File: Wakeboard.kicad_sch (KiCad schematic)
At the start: 30 parts, among them CN1 JST S2B-PH-SM4-TB(LF)(SN), J2 HCTL HC-TYPE-C-16P-01A, Q1 DMP2045UQ-7, SW1 TS-1088-AR02016, SW2 TS-1088-AR02016, U1 RT9080-33GJ5, U2 ESP32-S3-MINI-1, U3 LIS3DHTR_C15134, U4 MCP73831T-2ACI/OT

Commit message: PCB and Schematic v1.0
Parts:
- added C7: 10uF, Capacitor_SMD:C_0805_2012Metric, symbol Device:C
- added C8: 0.1uF, Capacitor_SMD:C_0805_2012Metric, symbol Device:C
- added TP1, TP2: TestPoint, TestPoint:TestPoint_Pad_D1.5mm, symbol Connector:TestPoint
- renumbered SW2 to SW1, SW1 to SW2
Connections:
- net 3.3V: now also C7.1, C8.1, TP2.1
- net GND: now also C7.2, C8.2
- net GPIO1: now also U2.5 (IO1); no longer U2.15 (IO11)
- net at C1.1, D1.1 (K), Q1.2 (S)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: now also TP1.1

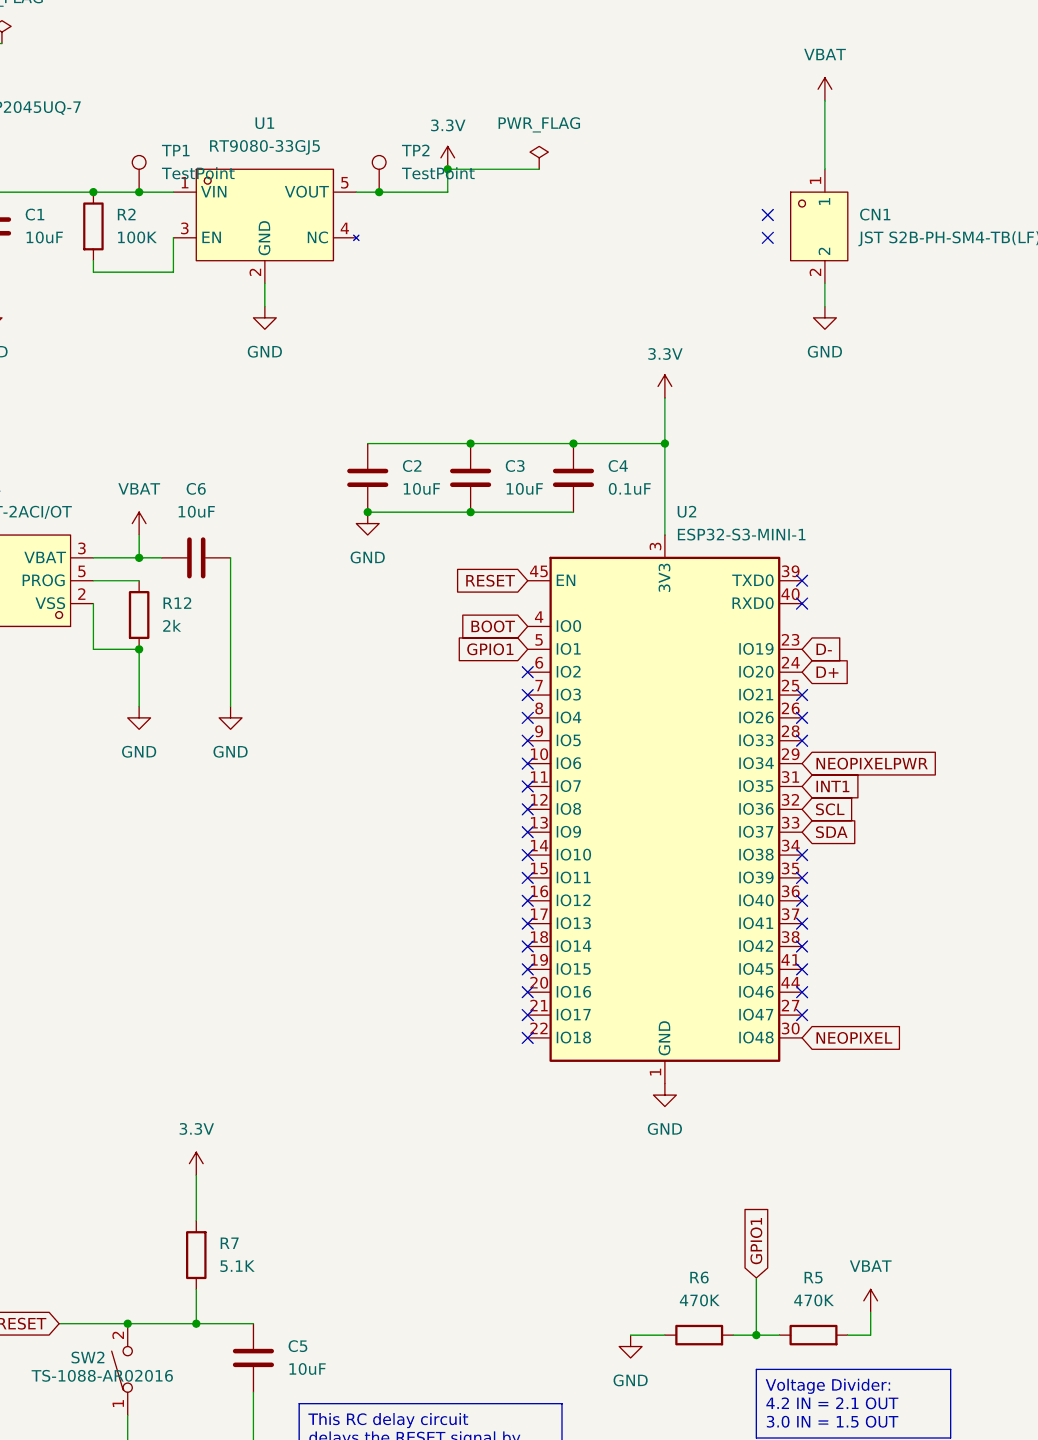
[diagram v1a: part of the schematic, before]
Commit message: Remove PCB below antenna. Swap SDA and SCL GPIO. Update interrupt to GPIO 21, battery level to GPIO 10.
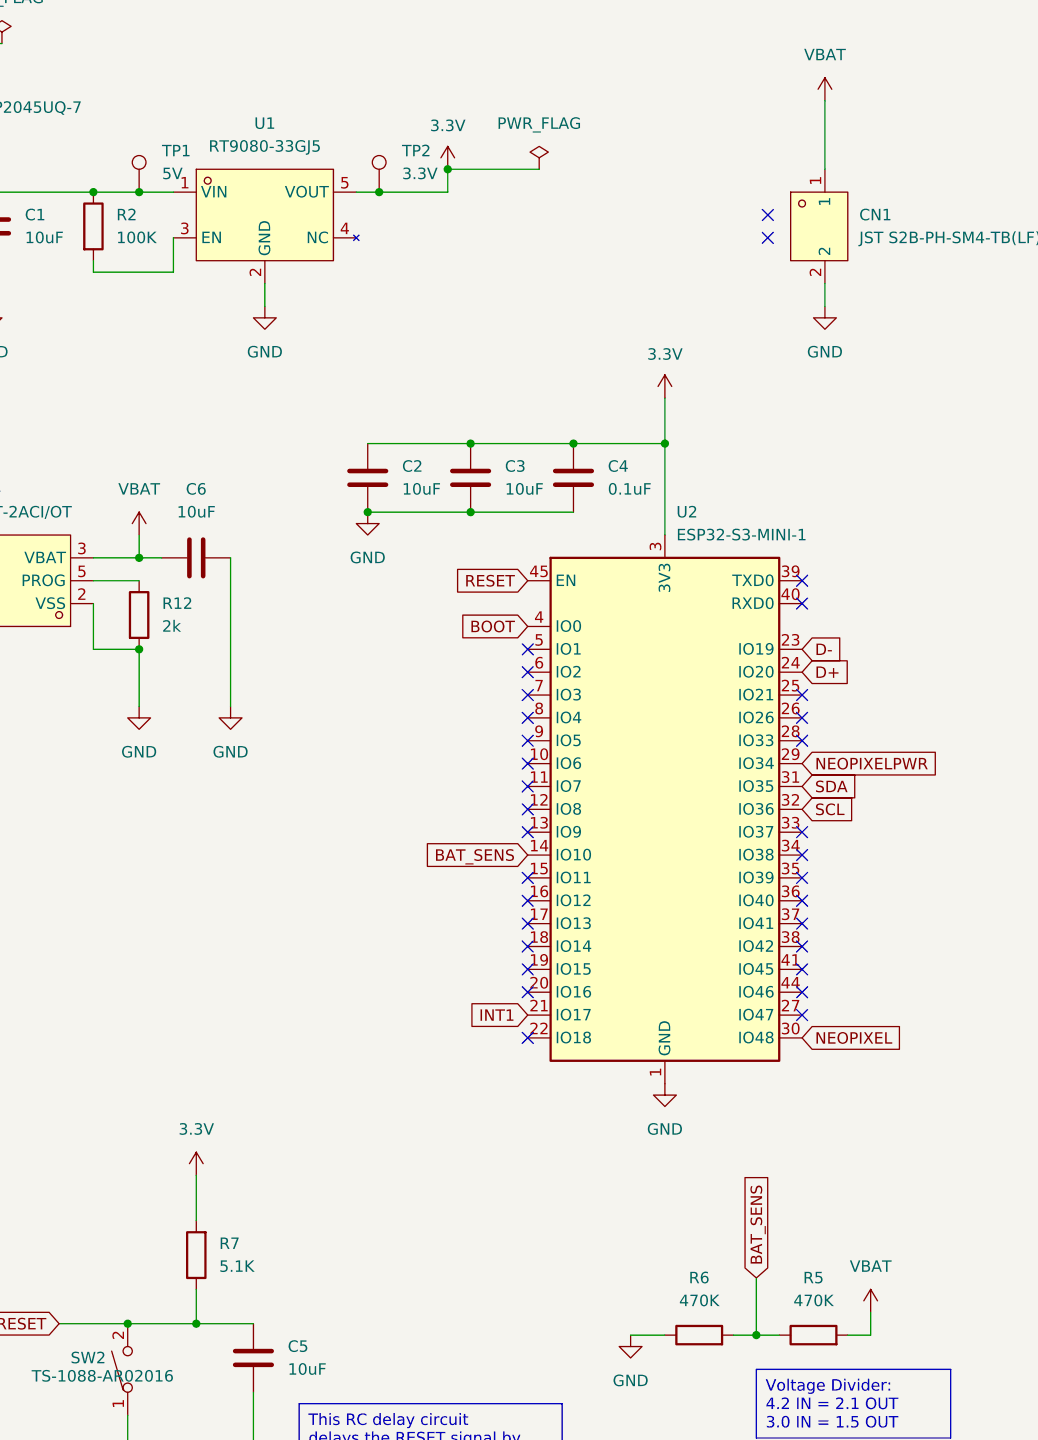
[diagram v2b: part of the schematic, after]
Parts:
- TP1: value TestPoint -> 5V
- TP2: value TestPoint -> 3.3V
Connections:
- net INT1: now also U2.21 (IO17); no longer U2.31 (IO35)
- net SDA: now also U2.31 (IO35); no longer U2.33 (IO37)
- net BAT_SENS: now reaches U2.14 (IO10)
- net BAT_SENS: now also R5.1, R6.2
- removed net GPIO1: R5.1, R6.2, U2.5 (IO1)
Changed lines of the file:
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@@
 	)
 	(no_connect
-		(at 107.95 130.81)
+		(at 138.43 110.49)
 	)
 	(no_connect
@@
 	)
 	(no_connect
+		(at 107.95 90.17)
+	)
+	(no_connect
 		(at 238.76 92.71)
 	)
@@
 	)
 	(no_connect
-		(at 107.95 113.03)
-	)
-	(no_connect
 		(at 138.43 85.09)
 	)
@@
 		)
 	)
-	(global_label "GPIO1"
+	(global_label "BAT_SENS"
 		(shape input)
 		(at 133.35 160.02 90)
@@
 		)
 		(property "Intersheetrefs" "${INTERSHEET_REFS}"
-			(at 133.35 151.35 90)
+			(at 133.35 147.8425 90)
 			(effects
 				(font
@@
 		)
 	)
-	(global_label "GPIO1"
+	(global_label "BAT_SENS"
 		(shape input)
-		(at 107.95 90.17 180)
+		(at 107.95 113.03 180)
 		(fields_autoplaced yes)
 		(effects
@@
 		)
 		(property "Intersheetrefs" "${INTERSHEET_REFS}"
-			(at 99.28 90.17 0)
+			(at 95.7725 113.03 0)
 			(effects
 				(font
@@
 	(global_label "INT1"
 		(shape input)
-		(at 138.43 105.41 0)
+		(at 107.95 130.81 180)
 		(fields_autoplaced yes)
 		(effects
@@
 				(size 1.27 1.27)
 			)
-			(justify left)
+			(justify right)
 		)
 		(property "Intersheetrefs" "${INTERSHEET_REFS}"
-			(at 145.5276 105.41 0)
+			(at 100.8524 130.81 0)
 			(effects
 				(font
 					(size 1.27 1.27)
 				)
-				(justify left)
+				(justify right)
 				(hide yes)
 			)
@@
 	(global_label "SDA"
 		(shape input)
-		(at 138.43 110.49 0)
+		(at 138.43 105.41 0)
 		(fields_autoplaced yes)
 		(effects
@@
 		)
 		(property "Intersheetrefs" "${INTERSHEET_REFS}"
-			(at 144.9833 110.49 0)
+			(at 144.9833 105.41 0)
 			(effects
 				(font
@@
 			)
 		)
-		(property "Value" "TestPoint"
+		(property "Value" "3.3V"
 			(at 93.98 37.3379 0)
 			(effects
@@
 			)
 		)
-		(property "Description" "test point"
+		(property "Description" "3.3V"
 			(at 91.44 39.37 0)
 			(effects
@@
 			)
 		)
-		(property "Value" "TestPoint"
+		(property "Value" "5V"
 			(at 67.31 37.3379 0)
 			(effects
@@
 			)
 		)
-		(property "Description" "test point"
+		(property "Description" "5V"
 			(at 64.77 39.37 0)
 			(effects

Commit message: Adding Gerber and BOM files
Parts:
- TP1, TP2: now not fitted
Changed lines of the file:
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@@
 		(in_bom yes)
 		(on_board yes)
-		(dnp no)
+		(dnp yes)
 		(fields_autoplaced yes)
 		(property "Reference" "TP2"
@@
 		(in_bom yes)
 		(on_board yes)
-		(dnp no)
+		(dnp yes)
 		(fields_autoplaced yes)
 		(property "Reference" "TP1"

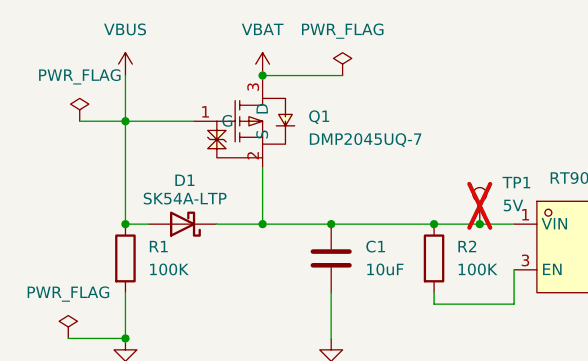
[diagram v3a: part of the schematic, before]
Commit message: Shift components after resize
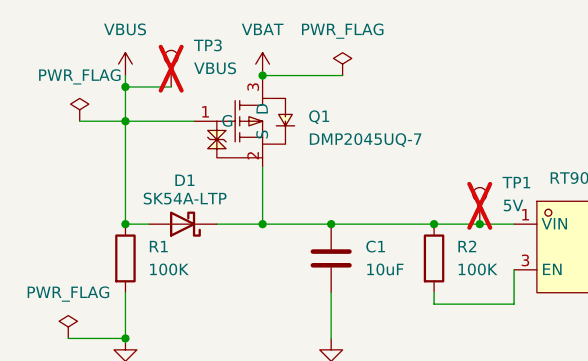
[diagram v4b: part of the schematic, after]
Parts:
- added TP3: VBUS, TestPoint:TestPoint_Pad_D1.5mm, symbol Connector:TestPoint
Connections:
- net VBUS: now also TP3.1
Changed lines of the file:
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@@
 	)
 	(junction
+		(at 25.4 24.13)
+		(diameter 0)
+		(color 0 0 0 0)
+	)
+	(junction
 		(at 198.12 100.33)
 		(diameter 0)
@@
 	(wire
 		(pts
+			(xy 25.4 24.13) (xy 25.4 27.94)
+		)
+		(stroke
+			(width 0)
+			(type default)
+		)
+	)
+	(wire
+		(pts
 			(xy 232.41 52.07) (xy 232.41 55.88)
 		)
@@
 	(wire
 		(pts
-			(xy 25.4 22.86) (xy 25.4 27.94)
+			(xy 25.4 22.86) (xy 25.4 24.13)
 		)
 		(stroke
@@
 	(wire
 		(pts
+			(xy 30.48 24.13) (xy 25.4 24.13)
+		)
+		(stroke
+			(width 0)
+			(type default)
+		)
+	)
+	(wire
+		(pts
 			(xy 140.97 49.53) (xy 140.97 52.07)
 		)
@@
 					(unit 1)
 				)
+			)
+		)
+	)
+	(symbol
+		(lib_id "Connector:TestPoint")
+		(at 30.48 24.13 0)
+		(unit 1)
+		(exclude_from_sim no)
+		(in_bom yes)
+		(on_board yes)
+		(dnp yes)
+		(fields_autoplaced yes)
+		(property "Reference" "TP3"
+			(at 33.02 19.5579 0)
+			(effects
+				(font
+					(size 1.27 1.27)
+				)
+				(justify left)
+			)
+		)
+		(property "Value" "VBUS"
+			(at 33.02 22.0979 0)
+			(effects
+				(font
+					(size 1.27 1.27)
+				)
+				(justify left)
+			)
+		)
+		(property "Footprint" "TestPoint:TestPoint_Pad_D1.5mm"
+			(at 35.56 24.13 0)
+			(effects
+				(font
+					(size 1.27 1.27)
+				)
+				(hide yes)
+			)
+		)
+		(property "Datasheet" "~"
+			(at 35.56 24.13 0)
+			(effects
+				(font
+					(size 1.27 1.27)
+				)
+				(hide yes)
+			)
+		)
+		(property "Description" "VBUS"
+			(at 30.48 24.13 0)
+			(effects
+				(font
+					(size 1.27 1.27)
+				)
+				(hide yes)
+			)
+		)
+		(pin "1"
+		)
+		(instances
+			(project "Wakeboard"
+				(path "/5eaee857-86a0-4093-a821-4f3b8843739e"
+					(reference "TP3")
+					(unit 1)
+				)
